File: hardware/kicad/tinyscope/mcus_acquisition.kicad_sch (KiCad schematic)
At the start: 30 parts, among them J5 STM32H743, Q2 NMOS, SW1 SW_SPST, U12 STM32H743VITx, X1 25MHz, X2 32k768

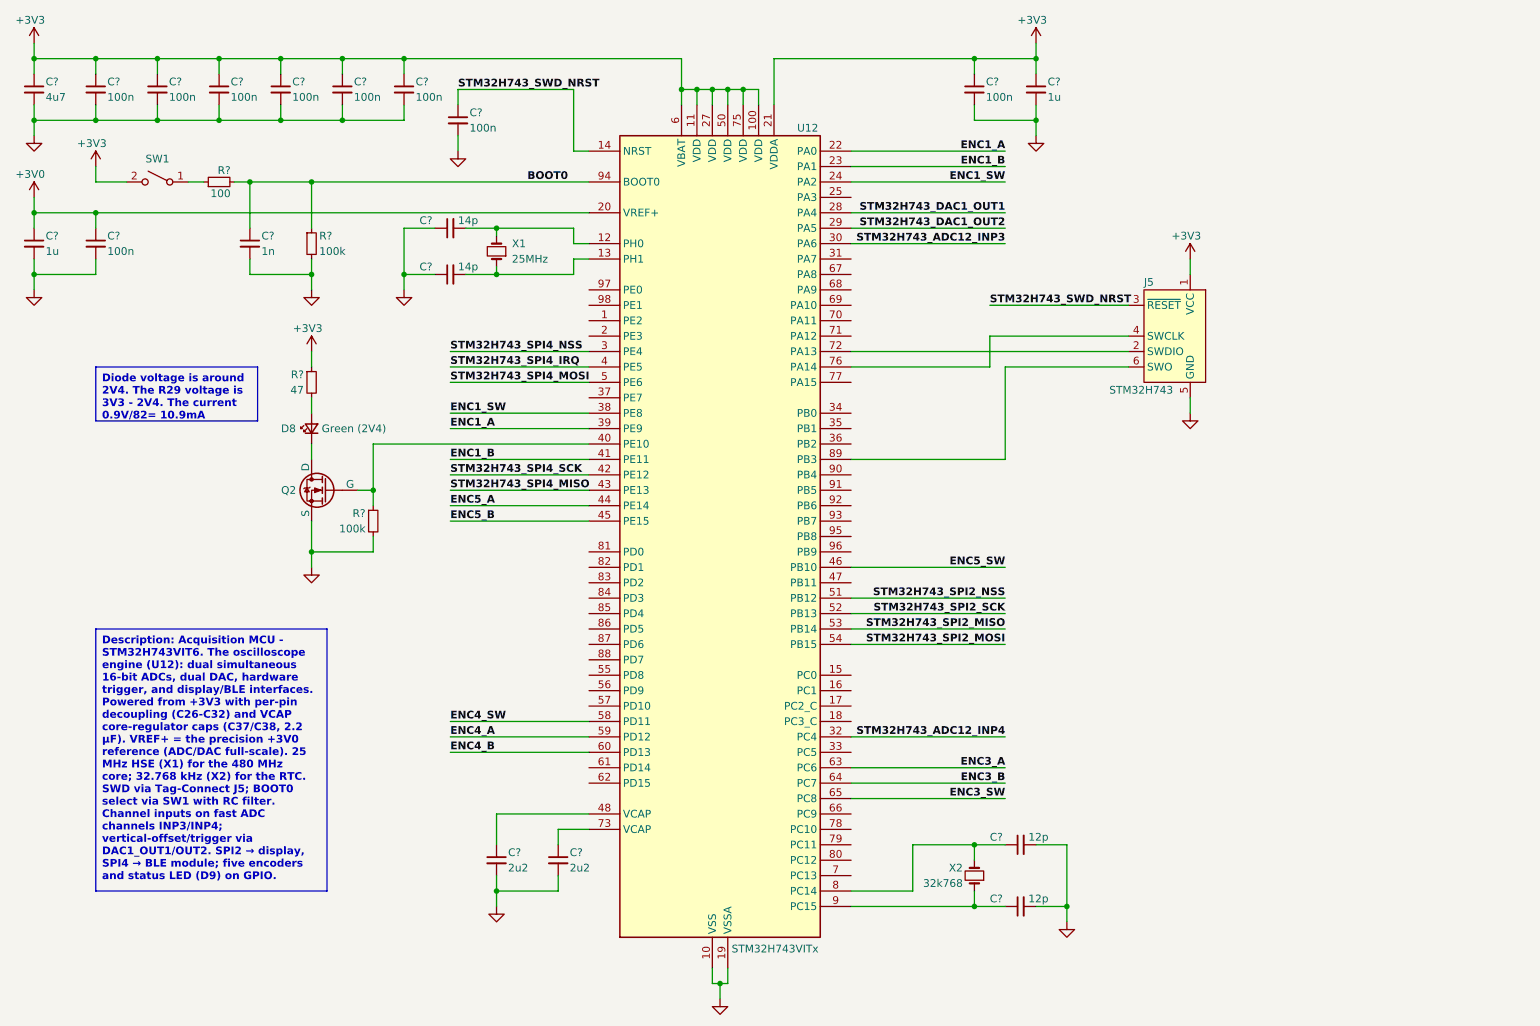
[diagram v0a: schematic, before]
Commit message: feat: hardware: Adds Waveshare 16498 display 02x17 connector. Cleans up all schematics
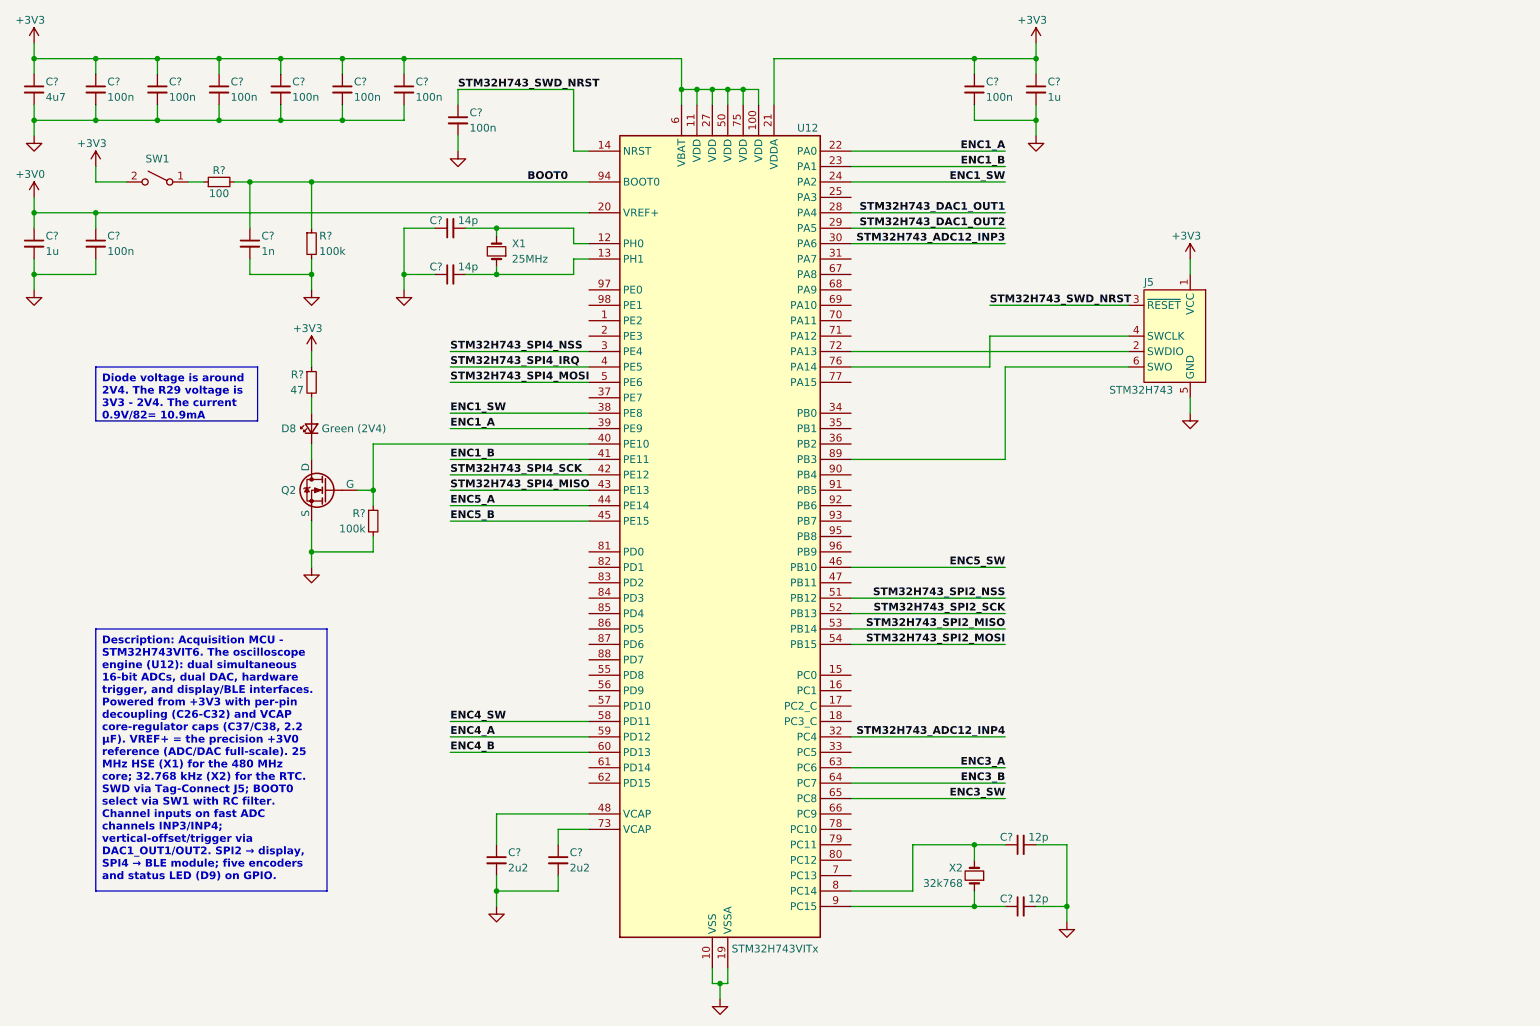
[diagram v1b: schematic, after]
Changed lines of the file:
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@@
   (symbol (lib_id "Device:C_Small") (at 111.76 48.26 90) (mirror x) (unit 1)
     (in_bom yes) (on_board yes) (dnp no)
-    (property "Reference" "C?" (at 106.68 46.99 90)
-      (effects (font (size 1.27 1.27)) (justify right))
+    (property "Reference" "C?" (at 110.49 46.99 90)
+      (effects (font (size 1.27 1.27)) (justify left))
     )
     (property "Value" "14p" (at 113.03 46.99 90)
@@
   (symbol (lib_id "Device:C_Small") (at 205.74 149.86 90) (mirror x) (unit 1)
     (in_bom yes) (on_board yes) (dnp no)
-    (property "Reference" "C?" (at 200.66 148.59 90)
-      (effects (font (size 1.27 1.27)) (justify right))
+    (property "Reference" "C?" (at 204.47 148.59 90)
+      (effects (font (size 1.27 1.27)) (justify left))
     )
     (property "Value" "12p" (at 207.01 148.59 90)
@@
   (symbol (lib_id "Device:C_Small") (at 111.76 55.88 90) (mirror x) (unit 1)
     (in_bom yes) (on_board yes) (dnp no)
-    (property "Reference" "C?" (at 106.68 54.61 90)
-      (effects (font (size 1.27 1.27)) (justify right))
+    (property "Reference" "C?" (at 110.49 54.61 90)
+      (effects (font (size 1.27 1.27)) (justify left))
     )
     (property "Value" "14p" (at 113.03 54.61 90)
@@
   (symbol (lib_id "Device:LED_Small") (at 88.9 81.28 90) (unit 1)
     (in_bom yes) (on_board yes) (dnp no)
-    (property "Reference" "D8" (at 85.09 81.28 90)
-      (effects (font (size 1.27 1.27)))
+    (property "Reference" "D8" (at 86.36 81.28 90)
+      (effects (font (size 1.27 1.27)) (justify left))
     )
     (property "Value" "Green (2V4)" (at 95.885 81.28 90)
@@
   (symbol (lib_id "Device:C_Small") (at 205.74 160.02 90) (mirror x) (unit 1)
     (in_bom yes) (on_board yes) (dnp no)
-    (property "Reference" "C?" (at 200.66 158.75 90)
-      (effects (font (size 1.27 1.27)) (justify right))
+    (property "Reference" "C?" (at 204.47 158.75 90)
+      (effects (font (size 1.27 1.27)) (justify left))
     )
     (property "Value" "12p" (at 207.01 158.75 90)
@@
   (symbol (lib_id "Device:R_Small") (at 73.66 40.64 90) (unit 1)
     (in_bom yes) (on_board yes) (dnp no)
-    (property "Reference" "R?" (at 75.565 38.735 90)
-      (effects (font (size 1.27 1.27)) (justify left))
-    )
-    (property "Value" "100" (at 75.565 42.545 90)
-      (effects (font (size 1.27 1.27)) (justify left))
+    (property "Reference" "R?" (at 73.66 38.735 90)
+      (effects (font (size 1.27 1.27)))
+    )
+    (property "Value" "100" (at 73.66 42.545 90)
+      (effects (font (size 1.27 1.27)))
     )
     (property "Footprint" "" (at 73.66 40.64 0)

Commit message: feat: hardware: doc: Modifies placement for the schematic description
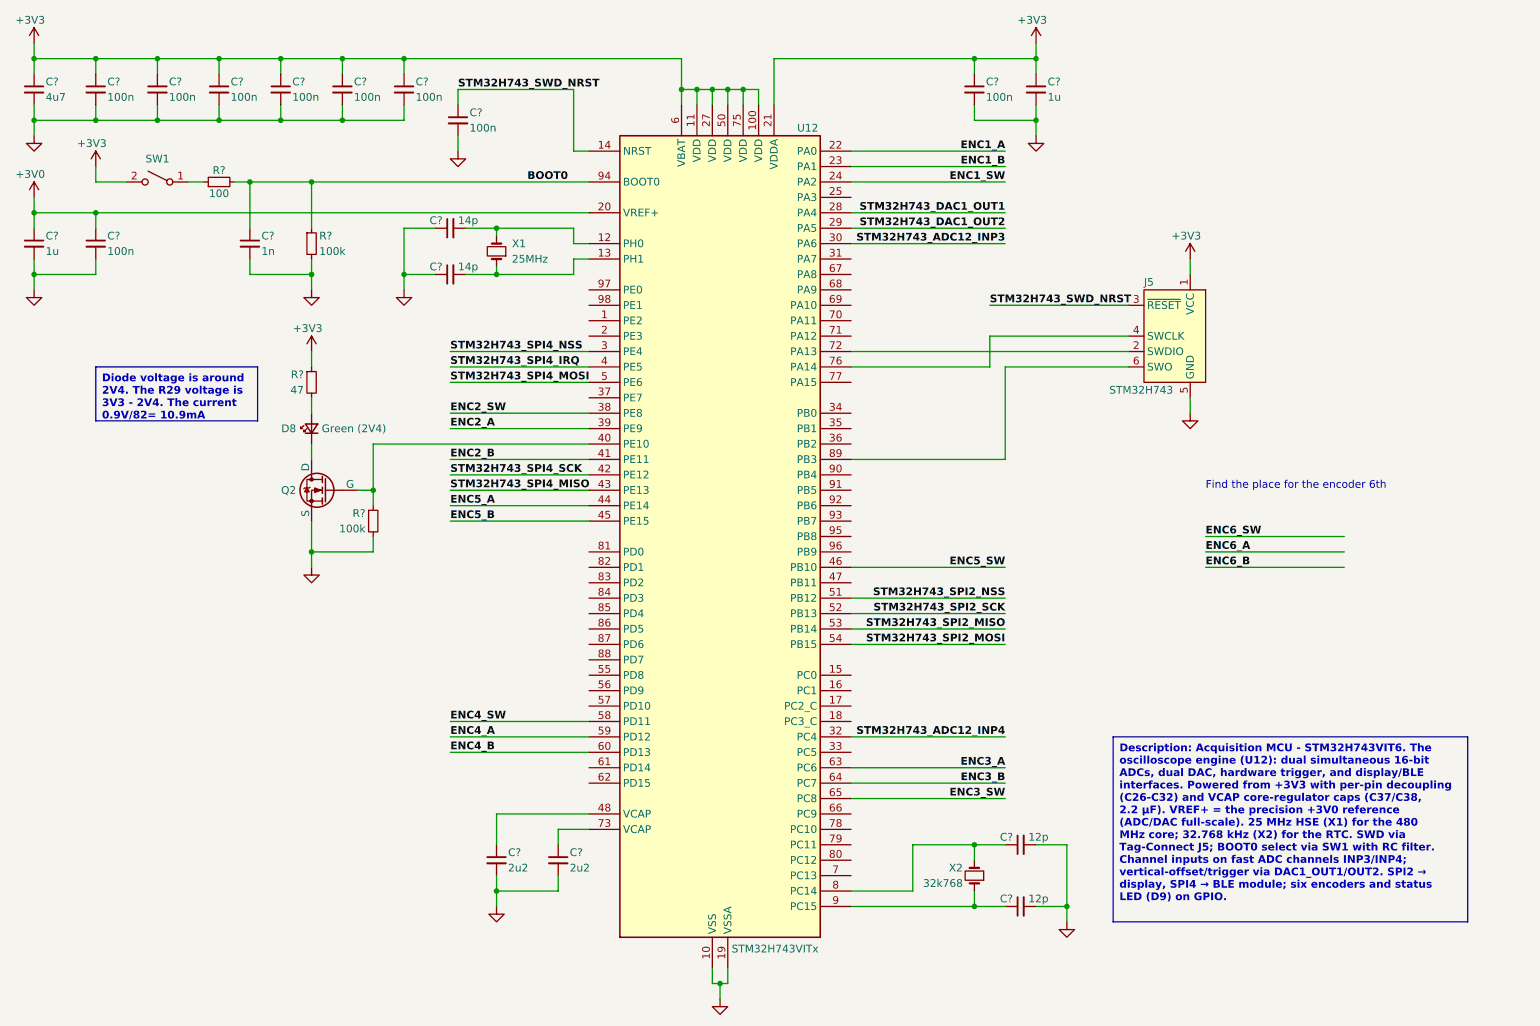
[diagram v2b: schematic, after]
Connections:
- net ENC1_A: no longer U12.39 (PE9)
- net ENC1_B: no longer U12.41 (PE11)
- net ENC1_SW: no longer U12.38 (PE8)
- new net ENC2_A: U12.39 (PE9)
- new net ENC2_B: U12.41 (PE11)
- new net ENC2_SW: U12.38 (PE8)
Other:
- note added: "Find the place for the encoder 6th"
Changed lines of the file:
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@@
+    (stroke (width 0) (type default))
+  )
+  (wire (pts (xy 259.08 99.06) (xy 236.22 99.06))
     (stroke (width 0) (type default))
   )
@@
   )
   (wire (pts (xy 177.8 104.14) (xy 203.2 104.14))
+    (stroke (width 0) (type default))
+  )
+  (wire (pts (xy 259.08 101.6) (xy 236.22 101.6))
+    (stroke (width 0) (type default))
+  )
+  (wire (pts (xy 259.08 104.14) (xy 236.22 104.14))
     (stroke (width 0) (type default))
   )
@@
     (effects (font (size 1.27 1.27) (thickness 0.254) bold) (justify left top))
   )
-  (text_box "Description: Acquisition MCU - STM32H743VIT6. The oscilloscope engine (U12): dual simultaneous 16-bit ADCs, dual DAC, hardware trigger, and display/BLE interfaces. Powered from +3V3 with per-pin decoupling (C26-C32) and VCAP core-regulator caps (C37/C38, 2.2 µF). VREF+ = the precision +3V0 reference (ADC/DAC full-scale). 25 MHz HSE (X1) for the 480 MHz core; 32.768 kHz (X2) for the RTC. SWD via Tag-Connect J5; BOOT0 select via SW1 with RC filter. Channel inputs on fast ADC channels INP3/INP4; vertical-offset/trigger via DAC1_OUT1/OUT2. SPI2 → display, SPI4 → BLE module; five encoders and status LED (D9) on GPIO."
-    (at 53.34 114.3 0) (size 38.1 43.18)
+  (text_box "Description: Acquisition MCU - STM32H743VIT6. The oscilloscope engine (U12): dual simultaneous 16-bit ADCs, dual DAC, hardware trigger, and display/BLE interfaces. Powered from +3V3 with per-pin decoupling (C26-C32) and VCAP core-regulator caps (C37/C38, 2.2 µF). VREF+ = the precision +3V0 reference (ADC/DAC full-scale). 25 MHz HSE (X1) for the 480 MHz core; 32.768 kHz (X2) for the RTC. SWD via Tag-Connect J5; BOOT0 select via SW1 with RC filter. Channel inputs on fast ADC channels INP3/INP4; vertical-offset/trigger via DAC1_OUT1/OUT2. SPI2 → display, SPI4 → BLE module; six encoders and status LED (D9) on GPIO."
+    (at 220.98 132.08 0) (size 58.42 30.48)
     (stroke (width 0) (type default))
     (fill (type color) (color 255 255 194 1))
     (effects (font (size 1.27 1.27) (thickness 0.254) bold) (justify left top))
   )
+  (text "Find the place for the encoder 6th" (at 236.22 91.44 0)
+    (effects (font (size 1.27 1.27)) (justify left bottom))
+  )
   (label "STM32H743_SWD_NRST" (at 113.03 25.4 0) (fields_autoplaced)
     (effects (font (size 1.27 1.27) bold) (justify left bottom))
@@
     (effects (font (size 1.27 1.27) bold) (justify right bottom))
   )
-  (label "ENC1_SW" (at 111.76 78.74 0) (fields_autoplaced)
+  (label "ENC2_SW" (at 111.76 78.74 0) (fields_autoplaced)
     (effects (font (size 1.27 1.27) bold) (justify left bottom))
   )
@@
     (effects (font (size 1.27 1.27) bold) (justify right bottom))
   )
+  (label "ENC6_SW" (at 236.22 99.06 0) (fields_autoplaced)
+    (effects (font (size 1.27 1.27) bold) (justify left bottom))
+  )
   (label "ENC3_B" (at 203.2 139.7 180) (fields_autoplaced)
     (effects (font (size 1.27 1.27) bold) (justify right bottom))
@@
     (effects (font (size 1.27 1.27) bold) (justify left bottom))
   )
+  (label "ENC6_A" (at 236.22 101.6 0) (fields_autoplaced)
+    (effects (font (size 1.27 1.27) bold) (justify left bottom))
+  )
   (label "ENC5_B" (at 111.76 96.52 0) (fields_autoplaced)
     (effects (font (size 1.27 1.27) bold) (justify left bottom))
@@
     (effects (font (size 1.27 1.27) bold) (justify right bottom))
   )
-  (label "ENC1_B" (at 111.76 86.36 0) (fields_autoplaced)
+  (label "ENC2_B" (at 111.76 86.36 0) (fields_autoplaced)
     (effects (font (size 1.27 1.27) bold) (justify left bottom))
   )
@@
     (effects (font (size 1.27 1.27) bold) (justify right bottom))
   )
-  (label "ENC1_A" (at 111.76 81.28 0) (fields_autoplaced)
-    (effects (font (size 1.27 1.27) bold) (justify left bottom))
-  )
+  (label "ENC6_B" (at 236.22 104.14 0) (fields_autoplaced)
+    (effects (font (size 1.27 1.27) bold) (justify left bottom))
+  )
+  (label "ENC2_A" (at 111.76 81.28 0) (fields_autoplaced)
+    (effects (font (size 1.27 1.27) bold) (justify left bottom))
+  )
